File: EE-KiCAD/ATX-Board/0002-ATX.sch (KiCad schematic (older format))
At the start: 19 parts, among them J101 Screw_Terminal_01x01, J102 Screw_Terminal_01x01, J103 Screw_Terminal_01x01, J104 Screw_Terminal_01x01, J105 Conn_01x03, J106 Conn_01x04

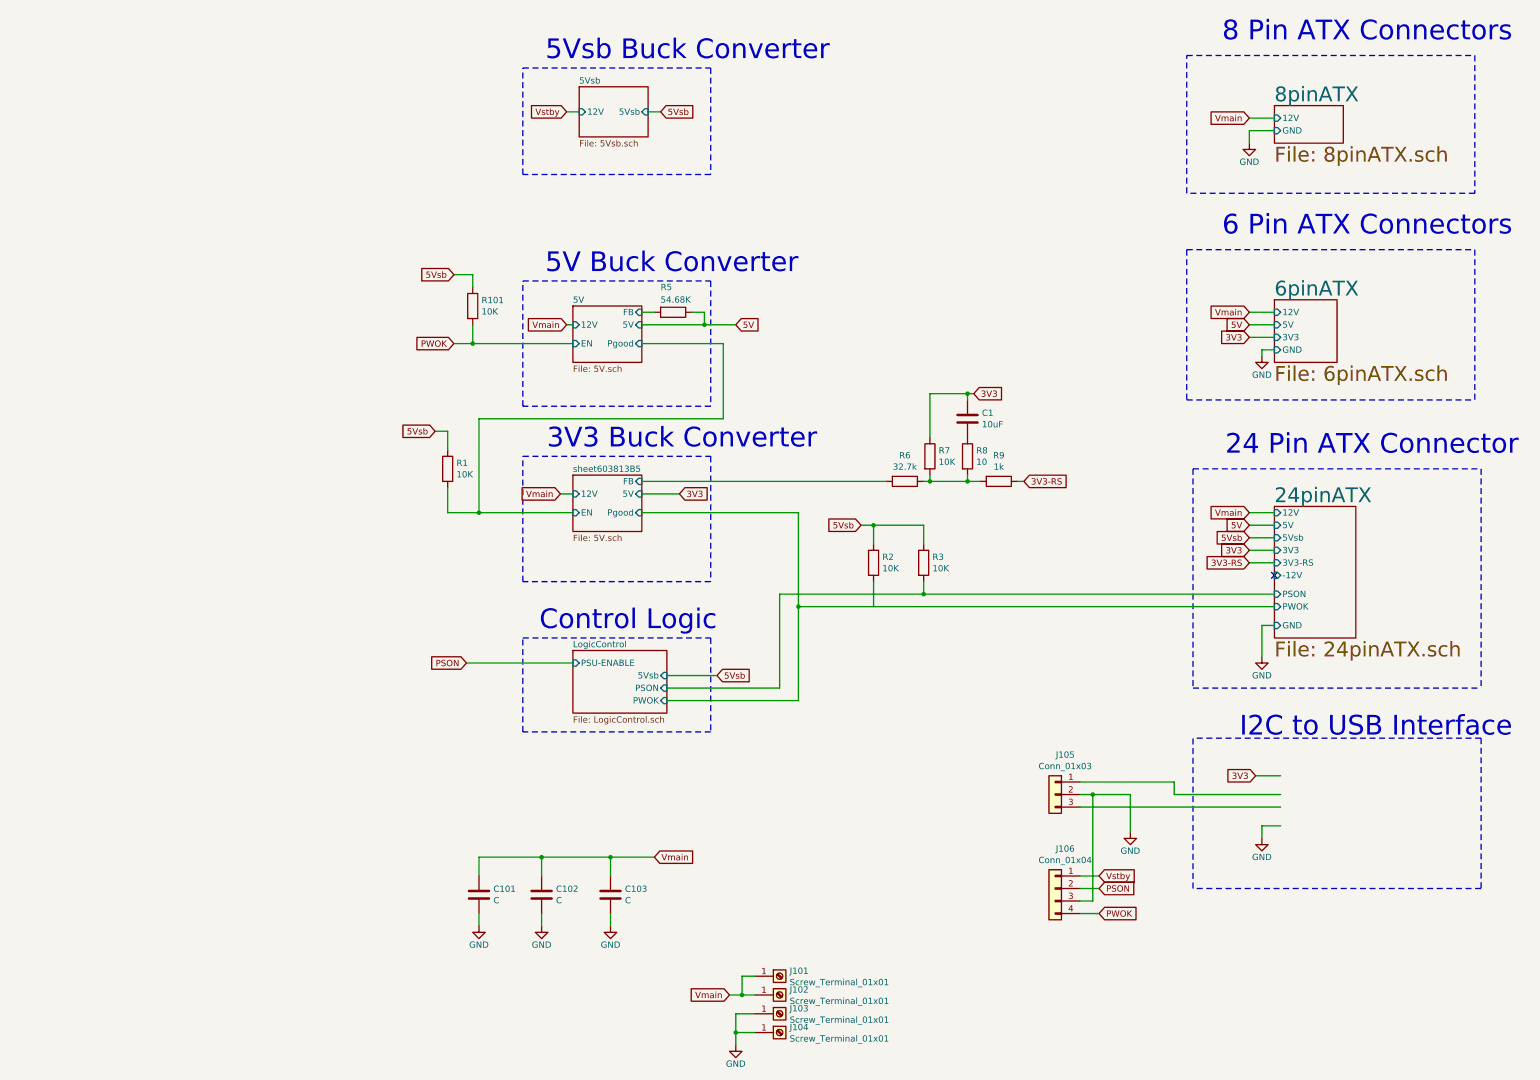
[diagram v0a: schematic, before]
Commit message: Finish first draft of PCBs.  Pulled PCBs into OpenSCAD for fitment.
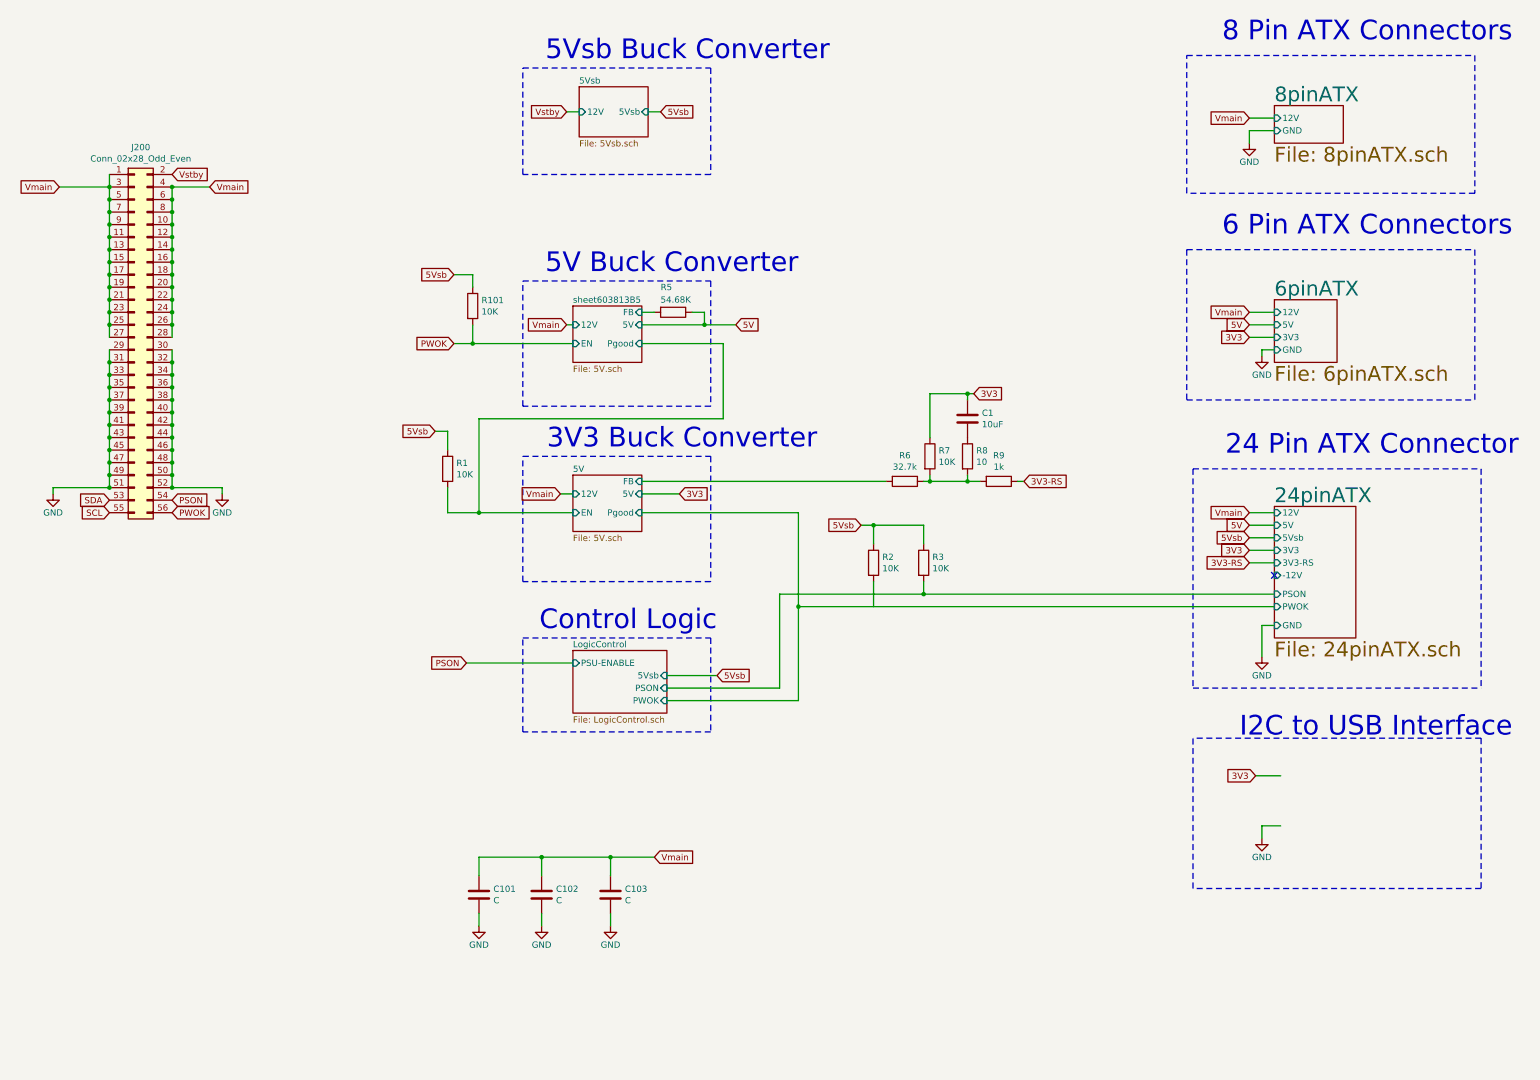
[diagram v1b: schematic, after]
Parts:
- removed J101, J102, J103, J104: Screw_Terminal_01x01, Mounting_Holes:MountingHole_5.3mm_M5_Pad_Via, symbol 0002-ATX-rescue:Screw_Terminal_01x01-conn
- removed J105: Conn_01x03, Connector_PinSocket_2.54mm:PinSocket_1x03_P2.54mm_Vertical, symbol 0002-ATX-rescue:Conn_01x03-conn
- removed J106: Conn_01x04, Connector_PinSocket_2.54mm:PinSocket_1x04_P2.54mm_Vertical, symbol 0002-ATX-rescue:Conn_01x04-conn
- added J200: Conn_02x28_Odd_Even, Connector_PinHeader_2.54mm:PinHeader_2x28_P2.54mm_Vertical, symbol Connector_Generic:Conn_02x28_Odd_Even
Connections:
- net labels added: SCL, SDA
- wire segments 99 -> 132

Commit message: add tabs on PCBs to set where they are in the box.  Box adjustments.
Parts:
- removed C1: 10uF, AEvan:0805_C, symbol Device:C
- removed C101, C102, C103: C, Capacitor_SMD:C_Elec_6.3x5.4, symbol Device:C
- removed R7: 10K, AEvan:0805_R, symbol Device:R
- removed R8: 10, AEvan:0805_R, symbol Device:R
- removed R9: 1k, AEvan:0805_R, symbol Device:R
- J200: footprint Connector_PinHeader_2.54mm:PinHeader_2x28_P2.54mm_Vertical -> Connector_PinSocket_2.54mm:PinSocket_2x28_P2.54mm_Horizontal
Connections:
- net 3V3: now also R6.1
- net PSON: now also J200.53 (Pin_53); no longer J200.54 (Pin_54)
- net PWOK: now also J200.55 (Pin_55); no longer J200.56 (Pin_56)
- net SCL: now also J200.56 (Pin_56); no longer J200.55 (Pin_55)
- net SDA: now also J200.54 (Pin_54); no longer J200.53 (Pin_53)
- net Vmain: now also J200.2 (Pin_2); no longer J200.1 (Pin_1)
- net Vstby: now also J200.1 (Pin_1); no longer J200.2 (Pin_2)
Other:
- moved on the sheet: R6
